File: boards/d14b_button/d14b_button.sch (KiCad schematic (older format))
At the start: 49 parts, among them CON1 USB-MICRO-B, P1 CONN_02X10, P2 CONN_01X03, SW1 SW_PUSH, SW2 SW_PUSH, SW3 SW_PUSH, U1 nRF24L01+-Module, U2 STM32F050C6, U3 TPS61221, X1 8M, X2 32.768k

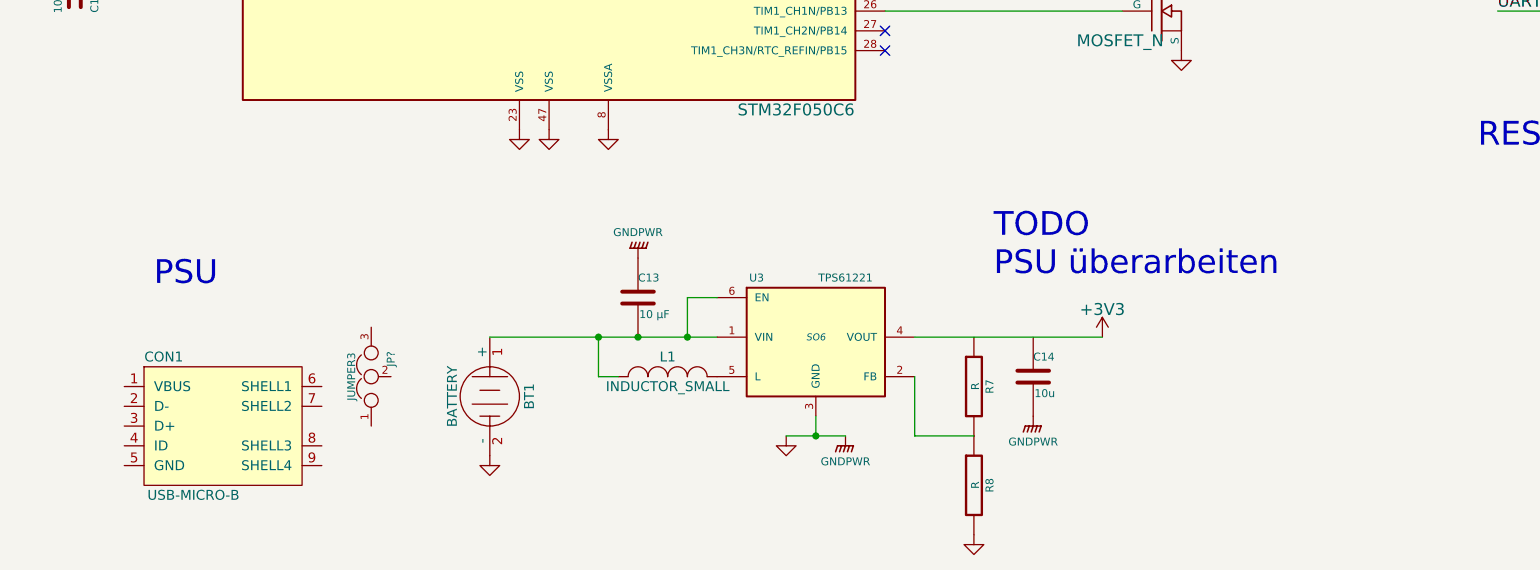
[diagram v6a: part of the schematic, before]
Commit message: PSU passt jetzt, USB fehlt noch
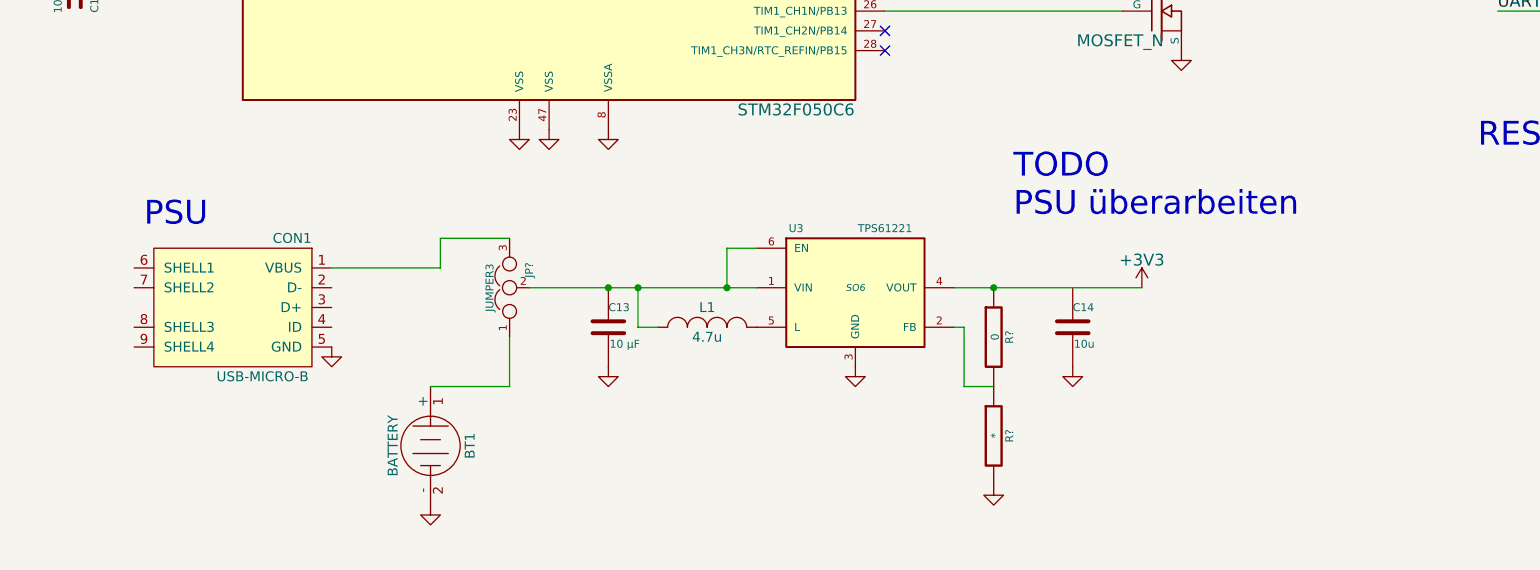
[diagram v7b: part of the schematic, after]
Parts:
- removed R7, R8: R, symbol R
- added R?: 0, symbol R
- added R?: *, symbol R
- L1: value INDUCTOR_SMALL -> 4.7u
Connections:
- net +3V3: now also R?.1
- net GND: now also C13.2, CON1.5 (GND), R?.2; no longer C13.1
- net at L1.1, U3.1 (VIN), U3.6 (EN): now also C13.1, JP?.2; no longer BT1.1 (+), C13.2
- net at CON1.1 (VBUS): now also JP?.3
- net at U3.2 (FB): now also R?.1, R?.2
- net at JP?.1: now also BT1.1 (+)
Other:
- moved on the sheet: BT1, C13, C14, CON1, JP?, L1, U3

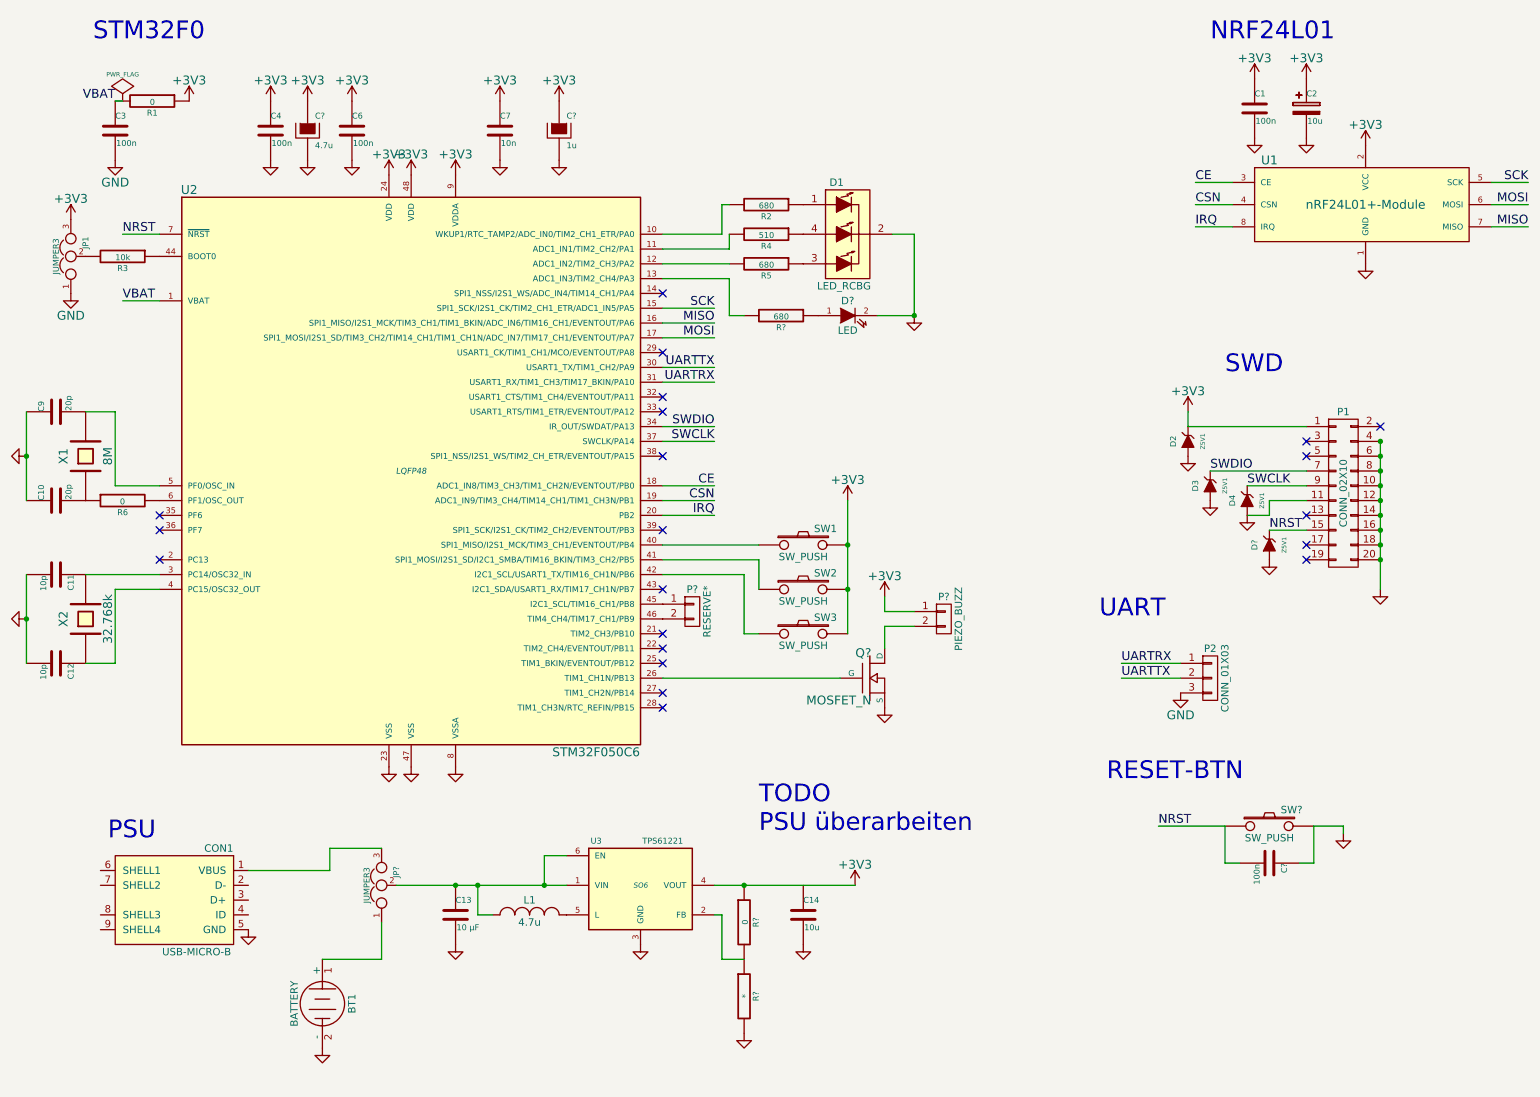
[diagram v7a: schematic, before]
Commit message: ERC erfolgreich abgeschlossen
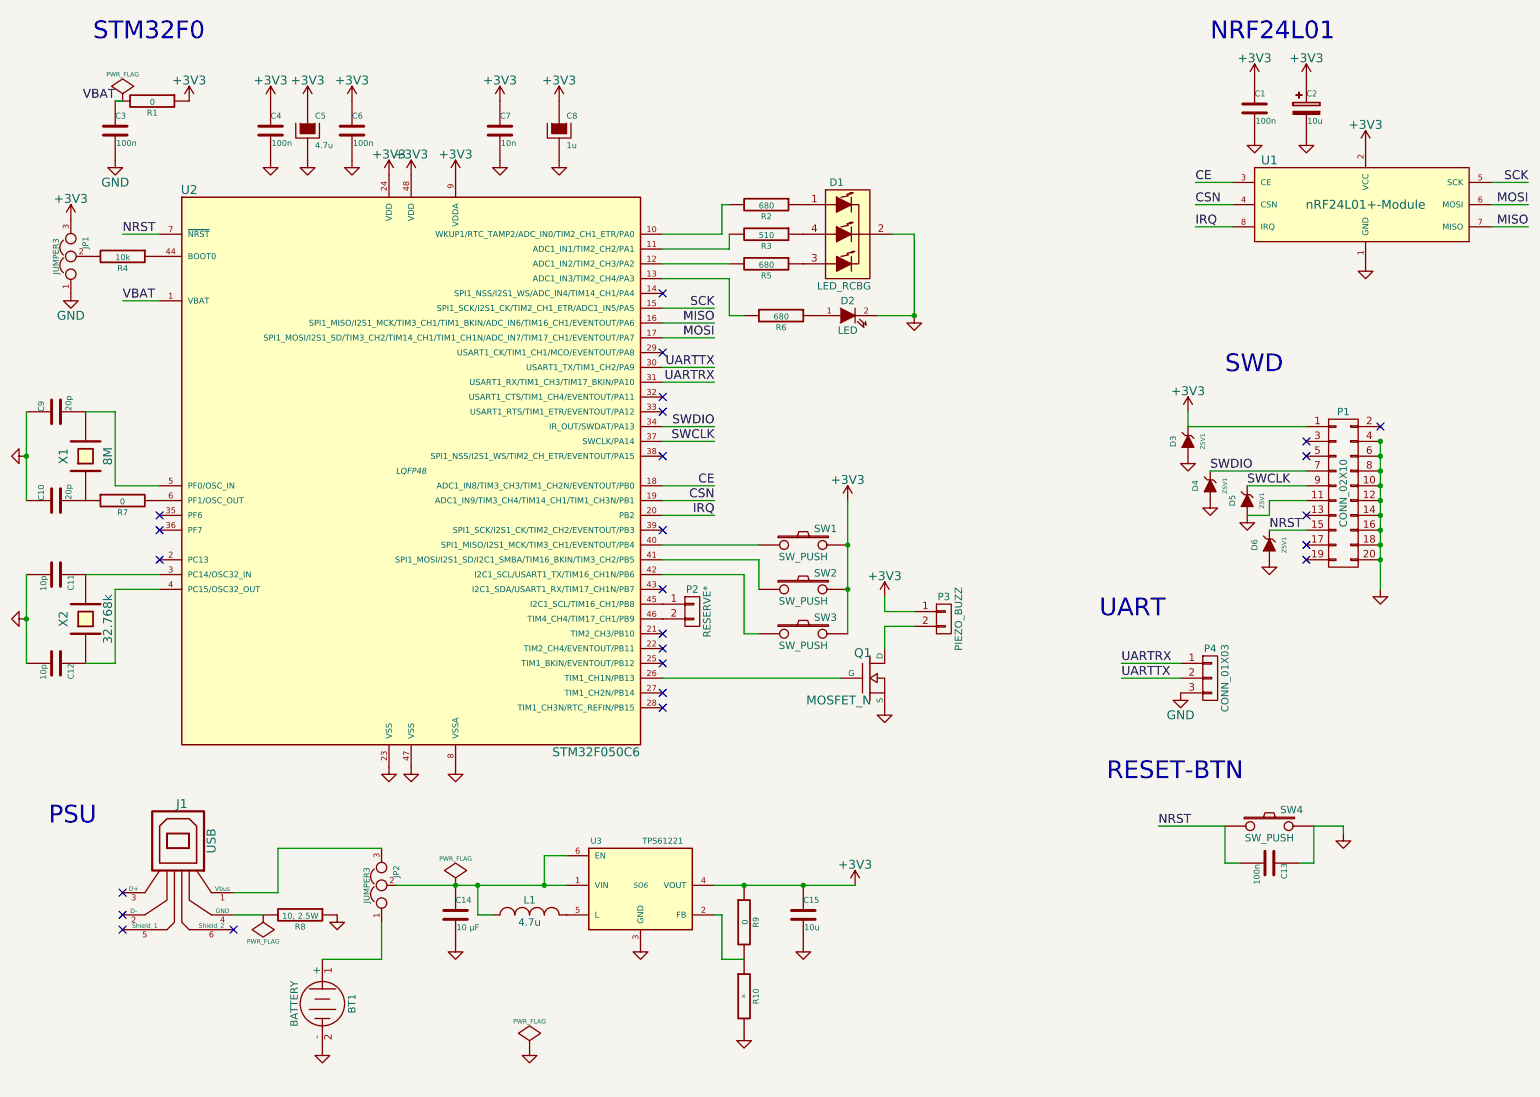
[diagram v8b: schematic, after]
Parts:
- removed CON1: USB-MICRO-B, symbol USB-MICRO-B
- added J1: USB, symbol USB
- added R8: 10, 2.5W, symbol R
- gave numbers to parts that had none: 13
- renumbered C13 to C14, C14 to C15, D2 to D3, D3 to D4, D4 to D5, P2 to P4, R4 to R3, R3 to R4, R6 to R7
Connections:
- net +3V3: now also C15.1
- net GND: now also R8.1
- net at JP2.3: now also J1.1 (Vbus)
- new net: J1.4 (GND), R8.2
- no-connect marks 21 -> 25
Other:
- note removed: "TODO\nPSU überarbeiten"
